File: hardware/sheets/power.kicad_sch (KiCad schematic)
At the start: 18 parts, among them J1 USB_C_Receptacle, U1 CH224K, U2 TPS563200

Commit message: JLCPCB sourcing pass: verify pinouts, LCSC part numbers, SMD build
Custom-symbol verification (open-questions Q5 resolved):
- MAX3241 symbol was wrong on nearly every pin and used MAX3243-style
  control names; regenerated to the real SSOP-28 pinout (SHDN#/EN#/
  R1OUTB/R2OUTB) and com_port rewired -- EN# must be GROUNDED (the old
  ~FORCEON-high would have disabled the receivers on real silicon)
- DS12C887 symbol wrong on 4 pins (DS=17, RESET#=18, IRQ#=19, SQW=23)

Sourcing (every part checked against the JLC DB; ~45 line items):
- New tools/parts.py maps (lib_id, value) -> LCSC; build.py applies it as
  an 'LCSC Part Num' property on every component (384 across the project)
- Sheets stay generic; stock-forced substitutions bound in the map:
  '374->'574 (parallel rewired), '163->'161, '157->HC157 (+HCT-buffered
  3.3V selects, I0/I1 swapped), '02->HC02, TCM809->MCP809, 2N3904->MMBT3904
- bus_mcu address counters moved to the 3.3V domain (HC161 on 3V3_BUS,
  loaded from MCU-side MD0-7; HCT244s read the 3.3V outputs at TTL Vih)
- 14.318 XOs are 3.3V-only parts: powered from 3V3, squared up via spare
  HCT gates (cpu_core U13, card_isatest U19)
- COM baud reference is now a 1.8432MHz crystal on the 16C550's XIN/XOUT
  (3.3V-only oscillators vs a 5V-only soft card)
- Supervisor QSPI header replaced with a real W25Q128JVSIQ
- Socket policy (fab installs sockets): V20 DIP-40, SRAM DIP-32 (no 5V
  512Kx8 SRAM at JLC at all), DS12C887 DIP-24, female headers for modules

Docs: CLAUDE.md fabrication-constraints section (SMD, 100x100mm, generic-
symbols rule, voltage-domain rule); README + hardware/README fab notes;
notes/jlcpcb-sourcing.md (decisions, thin-stock flags, not-at-JLC list);
stale questions-sidecar.md collapsed to its supersession record.

Rebuilt motherboard + cards: structural ERC 0, byte-identical rebuilds.

Co-Authored-By: Claude Fable 5 <noreply@anthropic.com>
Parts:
- C1, C3: LCSC Part Num (none) -> C12891
- C2, C4, C5: LCSC Part Num (none) -> C14663
- D1, D2: LCSC Part Num (none) -> C2286
- J1: LCSC Part Num (none) -> C2765186
- L1: LCSC Part Num (none) -> C602029
- R1, R2: LCSC Part Num (none) -> C23186
- R4, R6: LCSC Part Num (none) -> C25804
- R5: LCSC Part Num (none) -> C4216
- R7, R8: LCSC Part Num (none) -> C21190
- U1: LCSC Part Num (none) -> C970725
- U2: LCSC Part Num (none) -> C97253
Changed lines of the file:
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@@
+			)
+		)
+		(property "LCSC Part Num" "C2765186"
+			(at 50.8 165.1 0)
+			(effects
+				(font
+					(size 1.27 1.27)
+				)
+				(hide yes)
 			)
 		)
@@
 			)
 		)
+		(property "LCSC Part Num" "C23186"
+			(at 88.9 195.58 0)
+			(effects
+				(font
+					(size 1.27 1.27)
+				)
+				(hide yes)
+			)
+		)
 		(pin "1"
 		)
@@
 			)
 		)
+		(property "LCSC Part Num" "C23186"
+			(at 101.6 195.58 0)
+			(effects
+				(font
+					(size 1.27 1.27)
+				)
+				(hide yes)
+			)
+		)
 		(pin "1"
 		)
@@
 			)
 		)
+		(property "LCSC Part Num" "C970725"
+			(at 139.7 165.1 0)
+			(effects
+				(font
+					(size 1.27 1.27)
+				)
+				(hide yes)
+			)
+		)
 		(pin "7"
 		)
@@
 			)
 		)
+		(property "LCSC Part Num" "C25804"
+			(at 177.8 139.7 0)
+			(effects
+				(font
+					(size 1.27 1.27)
+				)
+				(hide yes)
+			)
+		)
 		(pin "1"
 		)
@@
 			)
 		)
+		(property "LCSC Part Num" "C12891"
+			(at 203.2 177.8 0)
+			(effects
+				(font
+					(size 1.27 1.27)
+				)
+				(hide yes)
+			)
+		)
 		(pin "1"
 		)
@@
 			)
 		)
+		(property "LCSC Part Num" "C14663"
+			(at 215.9 177.8 0)
+			(effects
+				(font
+					(size 1.27 1.27)
+				)
+				(hide yes)
+			)
+		)
 		(pin "1"
 		)
@@
 			)
 		)
+		(property "LCSC Part Num" "C97253"
+			(at 228.6 152.4 0)
+			(effects
+				(font
+					(size 1.27 1.27)
+				)
+				(hide yes)
+			)
+		)
 		(pin "3"
 		)
@@
 			)
 		)
+		(property "LCSC Part Num" "C14663"
+			(at 254 165.1 0)
+			(effects
+				(font
+					(size 1.27 1.27)
+				)
+				(hide yes)
+			)
+		)
 		(pin "1"
 		)
@@
 			)
 		)
+		(property "LCSC Part Num" "C602029"
+			(at 266.7 142.24 0)
+			(effects
+				(font
+					(size 1.27 1.27)
+				)
+				(hide yes)
+			)
+		)
 		(pin "1"
 		)
@@
 			)
 		)
+		(property "LCSC Part Num" "C4216"
+			(at 279.4 177.8 0)
+			(effects
+				(font
+					(size 1.27 1.27)
+				)
+				(hide yes)
+			)
+		)
 		(pin "1"
 		)
@@
 			)
 		)
+		(property "LCSC Part Num" "C25804"
+			(at 279.4 198.12 0)
+			(effects
+				(font
+					(size 1.27 1.27)
+				)
+				(hide yes)
+			)
+		)
 		(pin "1"
 		)
@@
 			)
 		)
+		(property "LCSC Part Num" "C12891"
+			(at 292.1 165.1 0)
+			(effects
+				(font
+					(size 1.27 1.27)
+				)
+				(hide yes)
+			)
+		)
 		(pin "1"
 		)
@@
 			)
 		)
+		(property "LCSC Part Num" "C14663"
+			(at 304.8 165.1 0)
+			(effects
+				(font
+					(size 1.27 1.27)
+				)
+				(hide yes)
+			)
+		)
 		(pin "1"
 		)
@@
 			)
 		)
+		(property "LCSC Part Num" "C21190"
+			(at 101.6 215.9 0)
+			(effects
+				(font
+					(size 1.27 1.27)
+				)
+				(hide yes)
+			)
+		)
 		(pin "1"
 		)
@@
 			)
 		)
+		(property "LCSC Part Num" "C2286"
+			(at 101.6 228.6 0)
+			(effects
+				(font
+					(size 1.27 1.27)
+				)
+				(hide yes)
+			)
+		)
 		(pin "1"
 		)
@@
 			)
 		)
+		(property "LCSC Part Num" "C21190"
+			(at 304.8 215.9 0)
+			(effects
+				(font
+					(size 1.27 1.27)
+				)
+				(hide yes)
+			)
+		)
 		(pin "1"
 		)
@@
 			(at 304.8 228.6 0)
 			(effects
+				(font
+					(size 1.27 1.27)
+				)
+				(hide yes)
+			)
+		)
+		(property "LCSC Part Num" "C2286"
+			(at 304.8 228.6 0)
+			(effects

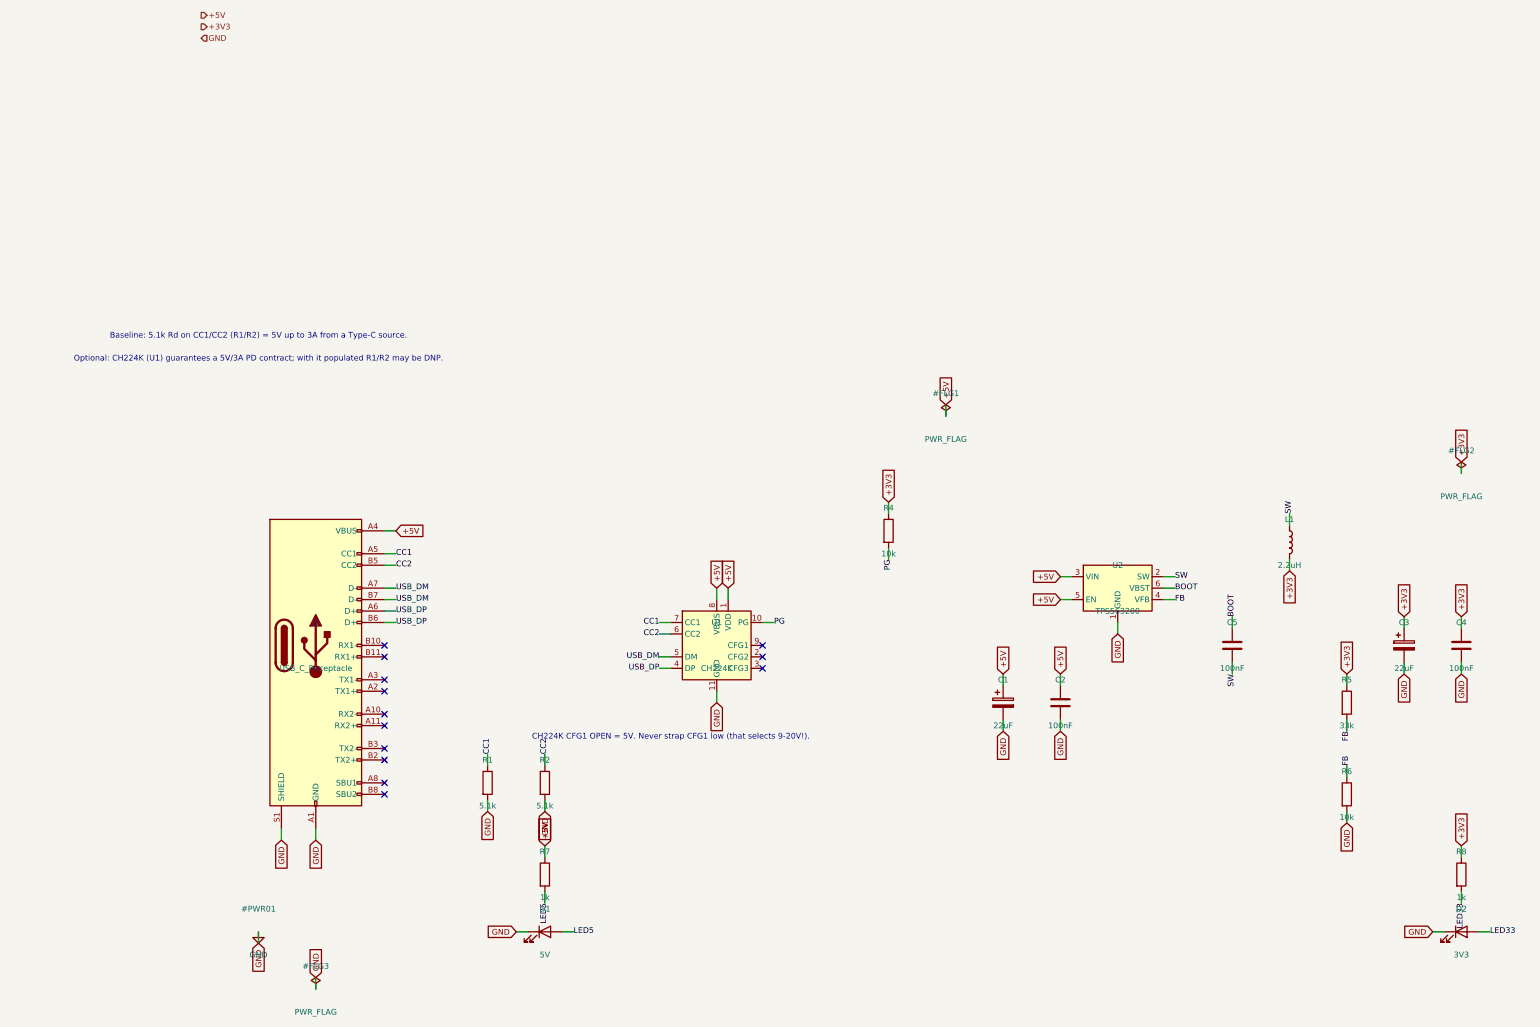
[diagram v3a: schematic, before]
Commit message: Design review 2026-07-11: rail protection, decoupling, wiring fixes
Protection:
- Sidecar +5V now feeds through a 2A polyfuse into +5V_ISA with an
  SMBJ5.0A clamp + 22uF bulk (a faulted ISA card trips its own fuse
  instead of dropping the board; back-fed voltage is clamped).
- USB-C VBUS enters through a 3A polyfuse with an SMBJ5.0A on +5V
  (backstop for the CFG1 9-20V failure mode). CH224K gains a 1uF VDD
  cap; its PG routes to Supervisor GPIO16 as PD_PG. Buck output
  doubled to 2x22uF, 10uF at VIN, extra rail bulk.
- Supervisor USB-A host port: 27R series termination (RP2040
  requirement), USBLC6-2SC6 ESD array, 100uF VBUS bulk.
- Video: HDMI +5V fused (500mA), HPD sensed on GPIO41, 100R series on
  VGA sync. TMDS ESD array deferred to layout (no symbol).
- card_isatest: V5RAW bulk, Q1 gate soft-start cap, TVS on DUT rail.

Wiring fixes:
- SPKR had no driver anywhere (netlist: 1 node). Bus MCU GPIO22
  reassigned from the diagnostics-only bus-CLK sense to SPKR; bus_mcu
  drops CLK from its interface. Doc 5.2 updated.
- bus_mcu C8 decoupled +3V3, a rail that sheet never uses -> 3V3_BUS.
- Storage IRQ5 was push-pull (permanently driven when idle) -> 2N7002
  + gated '125 tri-state, same convention as the LPT IRQ7 stage.
- MAX3241 pump caps resized to the 5V datasheet values (47nF/330nF).
- LPT DB25 status inputs get 4.7k pull-ups (floated with no printer).
- Audio line-out gets a 100R series isolator before the jack.

Best practices:
- Decoupling to ~1x100nF per IC on every sheet + bulk per board
  (cpu_core 7->16 incl. the naked 3.3V oscillator, storage 4->11,
  parallel 6->13, rtc/com/video/bus_mcu/card_isatest similar).
- All floating spare CMOS inputs tied ('00/'74/'157/'02/'04/'125
  sections across cpu_core, bus_mcu, rtc, storage, card_isatest).

Sourcing: new parts mapped in parts.py with JLC-verified LCSC numbers;
Power_Protection lib registered in the tools; TPS563200 stock alert
(4 pcs left at JLC) flagged in parts.py + jlcpcb-sourcing.md. All
decisi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
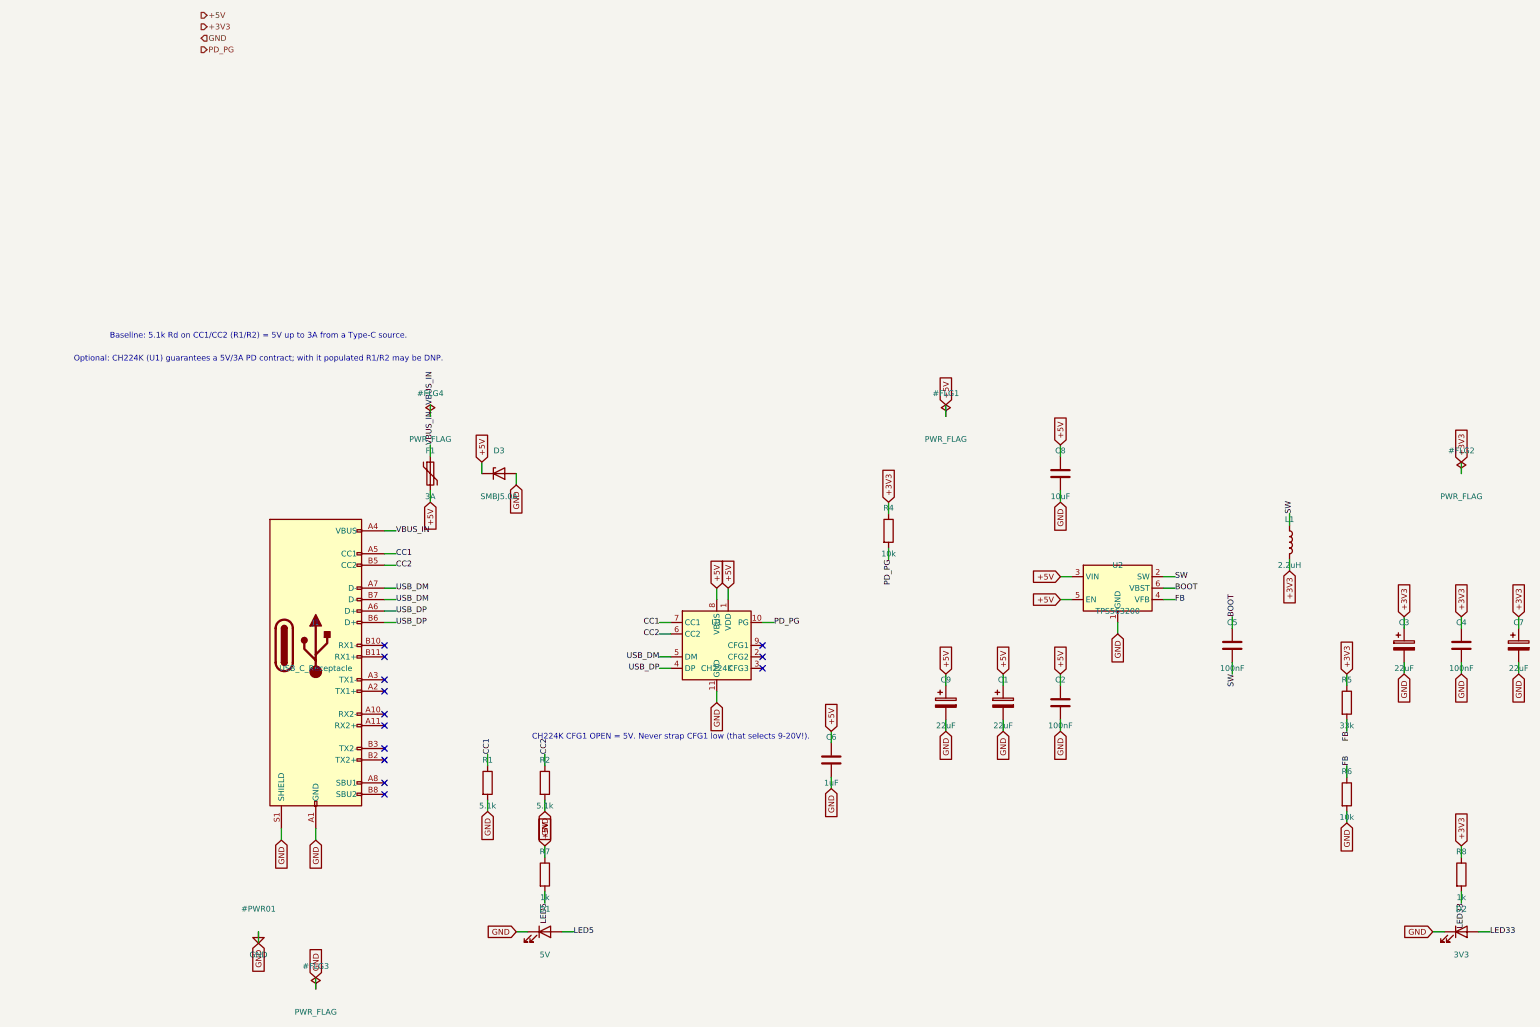
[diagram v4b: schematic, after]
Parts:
- added C6: 1uF, symbol Device:C
- added C7, C9: 22uF, symbol Device:C_Polarized
- added C8: 10uF, symbol Device:C
- added D3: SMBJ5.0A, symbol Device:D_Zener
- added F1: 3A, symbol Device:Polyfuse
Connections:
- net +3V3: now also C7.1
- net +5V: now also C6.1, C8.1, C9.1, D3.1 (K), F1.2; no longer J1.A4 (VBUS), J1.A9 (VBUS), J1.B4 (VBUS), J1.B9 (VBUS)
- net GND: now also C6.2, C7.2, C8.2, C9.2, D3.2 (A)
- net PG renamed PD_PG
- new net VBUS_IN: F1.1, J1.A4 (VBUS), J1.A9 (VBUS), J1.B4 (VBUS), J1.B9 (VBUS)
